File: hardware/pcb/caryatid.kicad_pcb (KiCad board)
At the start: 2 copper layers, 150 x 90 mm, 135 parts, among them J1 DC in, J10 FSR, J11 Digital bus, J12 RGB status, J13 Comms A - Qwiic, J14 Mic bias return, J15 Comms B - module, J16 Expansion / SPI1, J17 Audio out L/R/G, J18 Audio in L/R/rtn, J19 Comms A - module, J3 Latch switch, J4 Charge LEDs, J5 Analogue bus, J6 SW1 switch, J7 SW2 switch, J8 SW3 switch, J9 Soft pot, U1 BQ24074RGT, U2 TPS61023DRL, U3 74HC14, U4 MCP6002

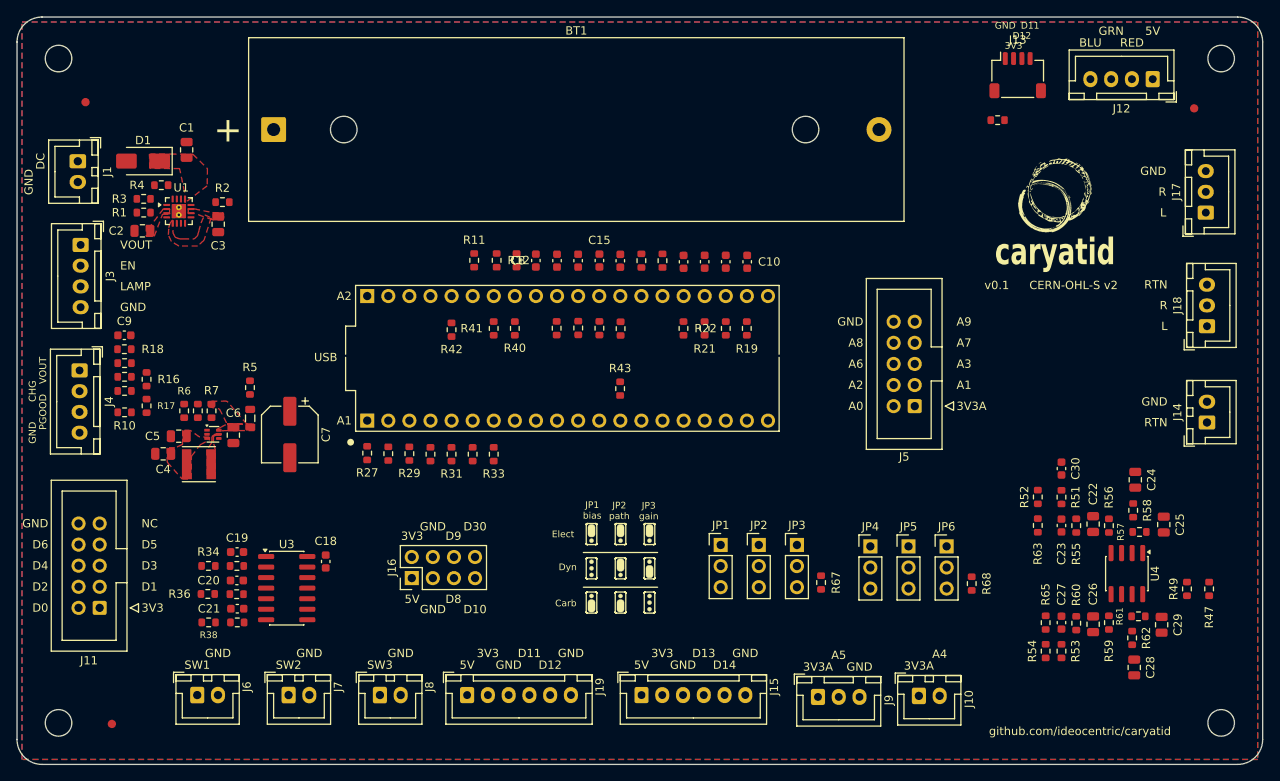
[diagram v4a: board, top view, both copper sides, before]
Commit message: Route the board: cycle.py, then hand routing to 4 unrouted
A full cycle.py run against the rebalanced placement, then hand routing
on top of it.

  stage                       real unrouted   pour islands   floating GND
  F.Cu only, no fanout            45              -              -
  + A1/A2 windows, -mt 1          30              -              -
  full cycle (with fanout)        25             12          924 mm2
  after hand routing               4              6          362 mm2

WHAT THE CYCLE ADDED OVER RUNNING THE PIECES BY HAND: fanout.py, which
recomputes fine-pitch escapes for wherever the parts now sit. Skipping it
left Freerouting's own fanout stage stalled at 52.8% of SMD pins escaped,
giving up after "no progress for 3 consecutive passes". With the escapes
pre-placed as 7 protected tracks, 25 rather than 30.

B.Cu STAYS A PLANE. --bcu-under A1,A2 declares it a signal layer and then
fences it with 13 keepouts, leaving windows only under the two 1x20 Seed
sockets -- 12.0% of the board open, the plane whole under the switcher
and the audio. Verified before trusting: all 40 socket pads inside a
window, none inside a keepout, which is the check af12deb records as
having once passed VACUOUSLY over an empty pad list.

The sockets are the bottleneck and the geometry says why: 2.54 mm pitch,
1.7 mm pads, 0.840 mm edge to edge, so after 0.2 mm clearance exactly ONE
0.25 mm track fits between neighbours, and forty pins each want it.

CARRIED OVER FROM THE ROUTER, AND BOTH WOULD FAIL FABRICATION:

  2 hole_clearance -- VBAT crosses BT1's NPTH at (89.345, 43.550) at
    0.000 mm against a 0.25 rule, twice, on 19.3 mm and 10.5 mm segments.
    The drill cuts the trace. Freerouting was never told the hole exists:
    the DSN cannot express drills, annular ring or hole-to-hole at all.
  11 track_width -- 0.1874 mm, one at 0.1250, against a 0.20 floor, on
    ISET, SW3_F, FB, TS, ILIM. All around U1/U2, so these are fanout's
    escapes rather than router output.

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
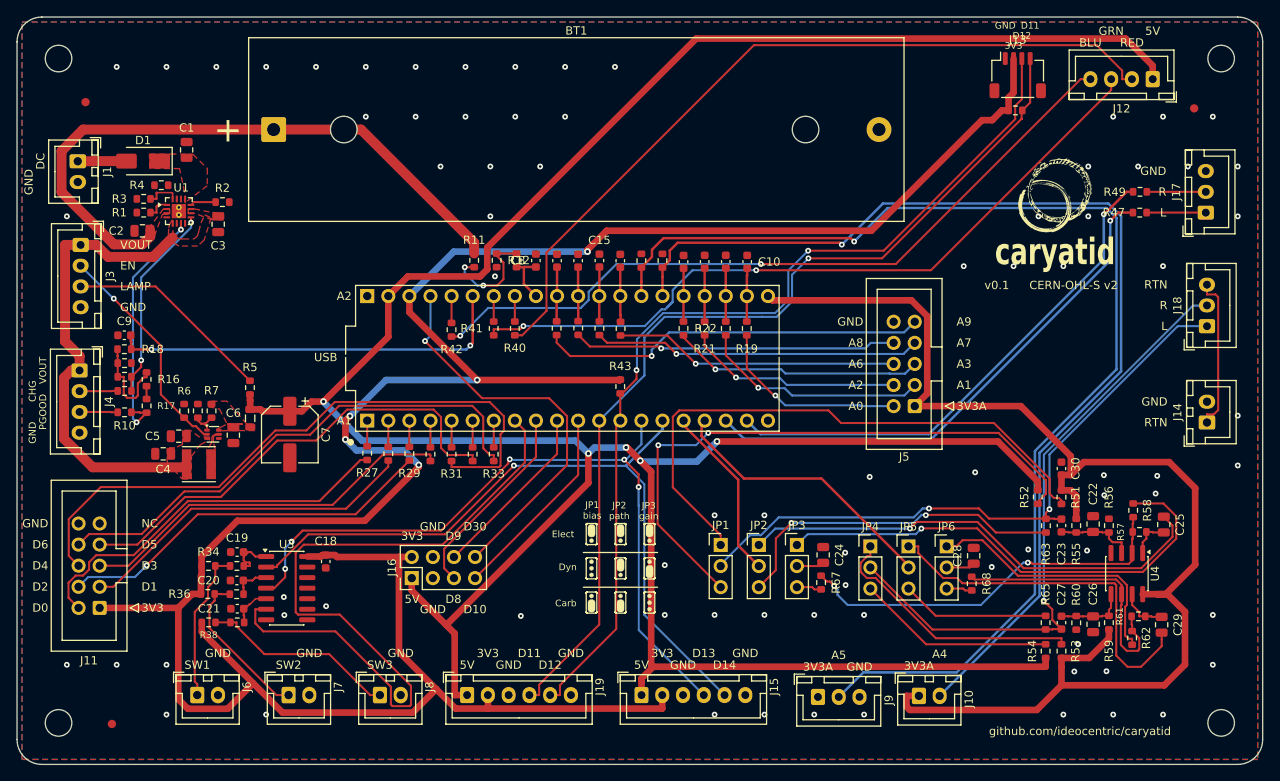
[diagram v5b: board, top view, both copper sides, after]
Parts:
- moved R49 48.1 mm to (185.2, 51.0), turned to 0 degrees
- moved R47 46.1 mm to (185.2, 53.5), turned to 0 degrees
- moved C24 38.7 mm to (147.1, 94.8)
- moved C28 23.6 mm to (165.2, 94.9), turned to 90 degrees
- moved R44 2.44 mm to (170.2, 41.2)
- moved R63 0.98 mm to (173.9, 91.2)
- moved R43 0.26 mm to (122.6, 74.5)
- turned R24 to 90 degrees
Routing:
- net +5V: track 0.00 -> 353.5 mm, vias 0 -> 5
- net +3V3: track 0.00 -> 315.7 mm, vias 0 -> 5
- net +3V3A: track 0.00 -> 157.3 mm
- net A5: track 0.00 -> 143.1 mm, vias 0 -> 1
- net A4: track 0.00 -> 130.2 mm, vias 0 -> 1
- net D11: track 0.00 -> 115.4 mm, vias 0 -> 1
- net D12: track 0.00 -> 114.3 mm, vias 0 -> 2
- net D14: track 0.00 -> 95.6 mm, vias 0 -> 1
- net /panel-io/RGB_R: track 0.00 -> 95.2 mm
- net D7: track 0.00 -> 91.8 mm
- net /panel-io/RGB_B: track 0.00 -> 90.4 mm, vias 0 -> 2
- net /panel-io/RGB_G: track 0.00 -> 90.1 mm, vias 0 -> 2
- net D13: track 0.00 -> 89.7 mm, vias 0 -> 5
- net /audio/MIC_L: track 0.00 -> 78.2 mm, vias 0 -> 2
- net /panel-io/D4_S: track 0.00 -> 77.9 mm
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
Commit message: Surgical re-route: VBAT clears BT1's hole, 4 unrouted -> 2
A cycle with all but two segments locked, so the hand routing that took
this board from 25 unrouted to 4 survives and only the defective copper
is replaced.

  real unrouted        4 -> 2
  hole_clearance       2 -> 0
  track_width         11 -> 12
  segments / vias    926/135 -> 938/148
  parity, stale_tracks   0, 0
  pour islands         6, 362 mm2 floating GND (unchanged)

THE HOLE FENCE IS NOW PROVEN END TO END. 844c90f made export_dsn.py emit
every non-plated hole as a keepout; this is a router honouring it. VBAT
routes around BT1's bolt hole instead of twice through it at 0.000 mm.
Geometry alone could not have shown that.

It also closed two connections it had in scope anyway -- +3V3A at J9 and
the TMR link R4.1 to U1.14.

STILL OPEN, and the second one is the one that matters:

  +3V3 at R14.1
  /power/SW pour -> U2 pad 5, ~0.29 mm short. The 1 MHz switching node,
  and now the only thing between this board and full connectivity.

widen_necks.py reverted again, correctly: widening the twelve necks
raised clearance 26 -> 34. They are load-bearing and want routing space,
not a wider track.

Copper is unlocked again -- 1058 released -- so the next full cycle
behaves normally.
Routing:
- net +3V3A: track 157.3 -> 170.2 mm
- net /power/TMR: track 0.00 -> 3.20 mm
- net /audio/MIC_L: track 78.2 -> 79.2 mm
- net /audio/VBIAS_R: track 8.47 -> 9.29 mm
- net VOUT: track 56.3 -> 55.8 mm
- net GND: vias 78 -> 91
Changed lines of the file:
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@@
 	)
 	(segment
+		(start 146.45 111.875)
+		(end 146.45 110.2483)
+		(width 0.8)
+		(layer "F.Cu")
+		(net 2)
+	)
+	(segment
 		(start 191.875 86.725)
 		(end 191.875 95.95)
@@
 	)
 	(segment
+		(start 146.45 110.2483)
+		(end 155.6006 110.2483)
+		(width 0.8)
+		(layer "F.Cu")
+		(net 2)
+	)
+	(segment
 		(start 190.65 107.975)
 		(end 190.65 101.625)
@@
 	)
 	(segment
+		(start 155.6006 110.2483)
+		(end 157.1003 111.748)
+		(width 0.8)
+		(layer "F.Cu")
+		(net 2)
+	)
+	(segment
 		(start 170.8736 76.855)
 		(end 176.8977 82.8791)
@@
 	)
 	(segment
+		(start 173.9 90.425)
+		(end 174.8853 90.425)
+		(width 0.25)
+		(layer "F.Cu")
+		(net 7)
+	)
+	(segment
 		(start 159.825 89.175)
 		(end 165.825 89.175)
@@
 		(net 7)
 	)
+	(segment
+		(start 174.8853 90.425)
+		(end 174.9113 90.399)
+		(width 0.25)
+		(layer "F.Cu")
+		(net 7)
+	)
 	(via
 		(at 159.825 89.175)
@@
 	(segment
 		(start 186.075 53.55)
+		(end 186.025 53.55)
+		(width 0.25)
+		(layer "F.Cu")
+		(net 14)
+	)
+	(segment
+		(start 186.075 53.55)
 		(end 193.146 53.55)
 		(width 0.25)
@@
 	)
 	(segment
+		(start 186.1 51.05)
+		(end 186.05 51.05)
+		(width 0.25)
+		(layer "F.Cu")
+		(net 15)
+	)
+	(segment
 		(start 186.075 51.025)
 		(end 186.1 51.05)
@@
 	)
 	(segment
+		(start 177.55 102.125)
+		(end 178.3057 102.125)
+		(width 0.25)
+		(layer "F.Cu")
+		(net 17)
+	)
+	(segment
 		(start 177.549 102.17)
 		(end 176.5887 102.17)
@@
 	)
 	(segment
+		(start 178.3057 102.125)
+		(end 178.3507 102.17)
+		(width 0.25)
+		(layer "F.Cu")
+		(net 17)
+	)
+	(segment
 		(start 179.581 102.172)
 		(end 180.6327 102.172)
@@
 	)
 	(segment
+		(start 68.2 50.25)
+		(end 68.9267 50.25)
+		(width 0.25)
+		(layer "F.Cu")
+		(net 51)
+	)
+	(segment
+		(start 69.7375 50.25)
+		(end 69.7375 51.9125)
+		(width 0.125)
+		(layer "F.Cu")
+		(net 51)
+	)
+	(segment
+		(start 68.9267 50.25)
+		(end 69.7375 50.25)
+		(width 0.25)
+		(layer "F.Cu")
+		(net 51)
+	)
+	(segment
 		(start 67.0502 52.5748)
 		(end 67.9748 52.5748)
@@
 	)
 	(via
+		(at 56 84)
+		(size 0.7)
+		(drill 0.3)
+		(layers "F.Cu" "B.Cu")
+		(net 91)
+	)
+	(via
+		(at 101 54)
+		(size 0.7)
+		(drill 0.3)
+		(layers "F.Cu" "B.Cu")
+		(net 91)
+	)
+	(via
 		(at 152 102)
 		(size 0.7)
@@
 	)
 	(via
+		(at 164 72)
+		(size 0.7)
+		(drill 0.3)
+		(layers "F.Cu" "B.Cu")
+		(net 91)
+	)
+	(via
 		(at 191 48)
 		(size 0.7)
@@
 	)
 	(via
+		(at 176 72)
+		(size 0.7)
+		(drill 0.3)
+		(layers "F.Cu" "B.Cu")
+		(net 91)
+	)
+	(via
 		(at 68 108)
 		(size 0.7)
@@
 	)
 	(via
+		(at 188 66)
+		(size 0.7)
+		(drill 0.3)
+		(layers "F.Cu" "B.Cu")
+		(net 91)
+	)
+	(via
 		(at 149.775 98.4)
 		(size 0.7)
@@
 	)
 	(via
+		(at 95 48)
+		(size 0.7)
+		(drill 0.3)
+		(layers "F.Cu" "B.Cu")
+		(net 91)
+	)
+	(via
 		(at 110.67 102.12)
 		(size 0.7)
@@
 	)
 	(via
+		(at 188 72)
+		(size 0.7)
+		(drill 0.3)
+		(layers "F.Cu" "B.Cu")
+		(net 91)
+	)
+	(via
 		(at 116 36)
 		(size 0.7)
@@
 	)
 	(via
+		(at 86 42)
+		(size 0.7)
+		(drill 0.3)
+		(layers "F.Cu" "B.Cu")
+		(net 91)
+	)
+	(via
 		(at 82.13 99.85)
 		(size 0.7)
@@
 	)
 	(via
+		(at 194 60)
+		(size 0.7)
+		(drill 0.3)
+		(layers "F.Cu" "B.Cu")
+		(net 91)
+	)
+	(via
 		(at 107 48)
 		(size 0.7)
@@
 	)
 	(via
+		(at 170 66)
+		(size 0.7)
+		(drill 0.3)
+		(layers "F.Cu" "B.Cu")
+		(net 91)
+	)
+	(via
 		(at 107 54)
 		(size 0.7)
@@
 	)
 	(via
+		(at 194 96)
+		(size 0.7)
+		(drill 0.3)
+		(layers "F.Cu" "B.Cu")
+		(net 91)
+	)
+	(via
 		(at 107.55 61.225)
 		(size 0.7)
@@
 	)
 	(via
+		(at 164 66)
+		(size 0.7)
+		(drill 0.3)
+		(layers "F.Cu" "B.Cu")
+		(net 91)
+	)
+	(via
 		(at 140 90)
 		(size 0.7)
@@
 	)
 	(via
+		(at 194 90)
+		(size 0.7)
+		(drill 0.3)
+		(layers "F.Cu" "B.Cu")
+		(net 91)
+	)
+	(via
 		(at 68 36)
 		(size 0.7)
@@
 	)
 	(segment
+		(start 83.3017 43.55)
+		(end 96.925 57.1733)
+		(width 1.2)
+		(layer "F.Cu")
+		(net 92)
+	)
+	(segment
 		(start 61.6616 57.3767)
 		(end 55.3637 51.0788)
@@
 	)
 	(segment
-		(start 55.3637 46.1448)
-		(end 57.9585 43.55)
+		(start 80.9 43.55)
+		(end 83.3017 43.55)
 		(width 1.2)
 		(layer "F.Cu")
@@
 	)
 	(segment
-		(start 91.4267 43.55)
-		(end 105.05 57.1733)
+		(start 55.3637 46.1448)
+		(end 57.9585 43.55)
 		(width 1.2)
 		(layer "F.Cu")
@@
 	)
 	(segment
-		(start 80.9 43.55)
-		(end 91.4267 43.55)
+		(start 96.925 57.1733)
+		(end 105.05 57.1733)
 		(width 1.2)
 		(layer "F.Cu")
@@
 		(width 1.2)
 		(layer "F.Cu")
-		(net 94)
-	)
-	(segment
-		(start 70.425 83.85)
-		(end 70.05 84.225)
-		(width 1.2)
-		(layer "F.Cu")

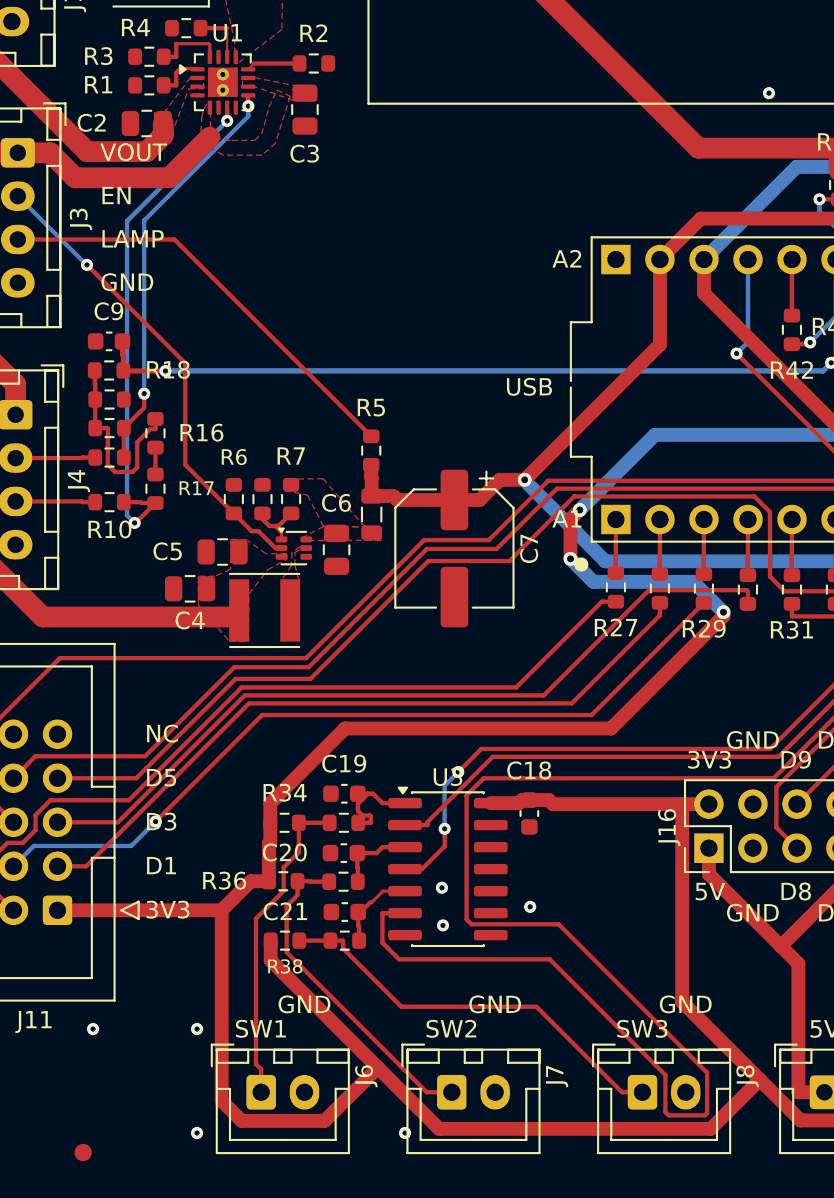
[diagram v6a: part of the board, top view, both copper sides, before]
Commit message: Route SW out of U2-5 into the channel; zero real unrouted connections
Your hand routing (22 tracks, 13 vias, no parts moved) plus the SW node,
which needed a track rather than a pour.

  real unrouted        2 -> 0
  clearance            0
  hole_clearance       0
  parity, stale_tracks 0, 0
  pour islands         6 -> 4

THE SW POUR WAS NEVER GOING TO REACH U2-5, and this was already written
down in fanout.py::pour_connects: the pour encloses both U2-5 and L1-2
but the only ways into U2-5 are the 0.150 mm gaps above and below it in
the pad column, and at the zone's 0.25 mm min_thickness the fill cannot
form a neck that narrow. So it bonds L1-2 and leaves U2-5 floating,
0.29 mm short. cycle.py::strip_copper records the remedy -- LEFT into
the channel between the pad columns, per SLVSF14B Figure 10-1, locked
because fanout only escapes radially and would never regenerate it.

  U2-5 (74.300, 80.250) --west--> (73.5875, 80.250)  0.20 mm  LOCKED
                        --south-> (73.5875, 82.600)  0.20 mm  LOCKED

Down the centre of the 0.745 mm channel, 0.55 mm into L1-2. Locked, so
a cycle keeps it and export_dsn emits it as (type protect).

IT DOES NOT WIDEN TO CLASS WIDTH, AND MY FIRST ATTEMPT WAS WRONG TO.
"Widen once clear of the package" sounds right and does not fit --
measured, 1.2 mm on this centre line OVERLAPS the VOUT pour by 0.18 mm
and both U2 pad columns by 0.23 mm:

    width   to VOUT pour   to U2-3    to U2-4
     0.2      +0.3175      +0.2725    +0.2725
     1.2      -0.1825      -0.2275    -0.2275

DRC caught it. And widening buys nothing regardless: L1-2 is 1.15 x 3.60
mm of solid copper, so once the track lands the PAD is the conductor.

I ALSO ARGUED FOR A CLEARANCE EXCEPTION THAT WAS ALREADY MADE. I
predicted three violations at 0.2725 against HighCurrent's 0.30 and
reasoned that 0.30 is unachievable on a package whose own pads sit
0.150 mm apart. The reasoning holds; the conclusion was redundant. U2
already carries a LOCAL CLEARANCE OVERRIDE O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
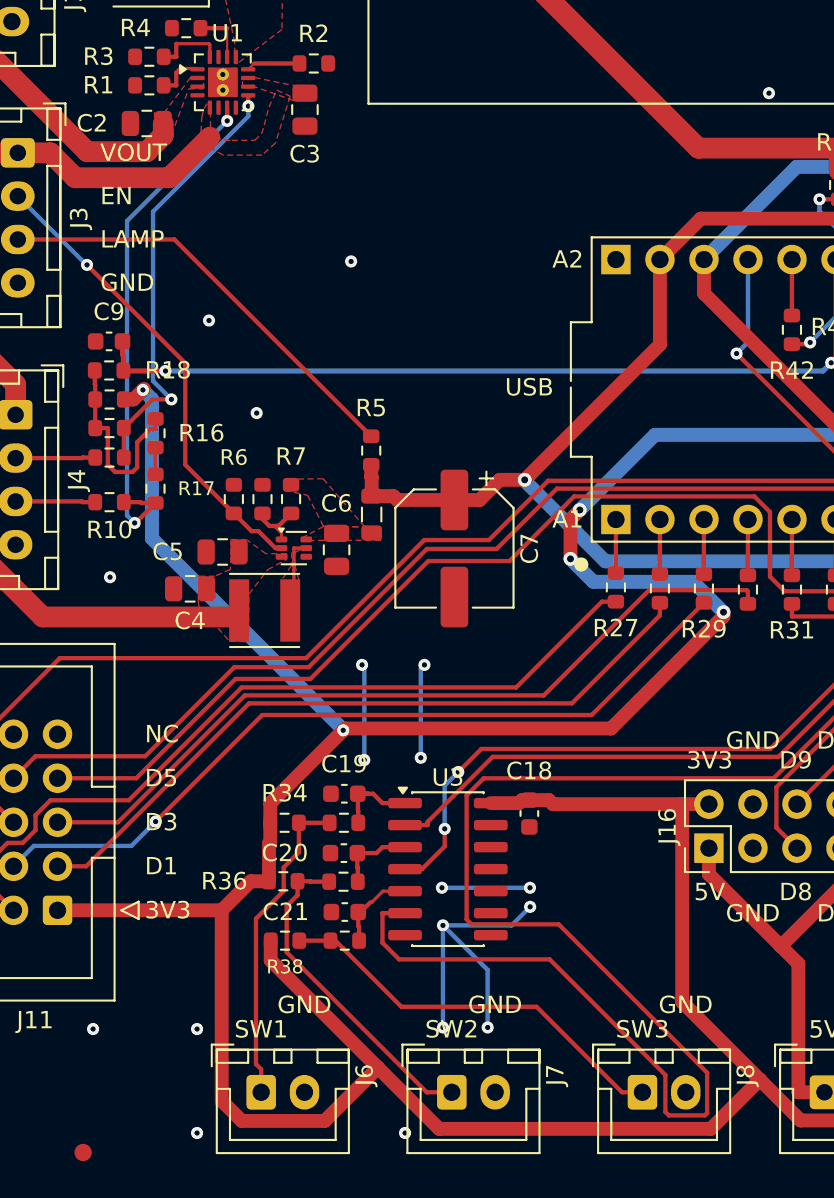
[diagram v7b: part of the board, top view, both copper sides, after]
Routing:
- net GND: track 0.00 -> 34.4 mm, vias 91 -> 102
- net +3V3: track 315.7 -> 341.6 mm, vias 5 -> 7
- net /power/SW: track 0.00 -> 3.06 mm
- net ~{CHG}: track 23.9 -> 25.4 mm
- net /panel-io/SW1_F: track 6.15 -> 5.21 mm
